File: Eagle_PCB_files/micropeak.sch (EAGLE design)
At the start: 2 parts, among them U1 ATTINY85-20MUR

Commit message: added schematic sheet template
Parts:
- added BT1: BHX1-1025-SM, BHX1-1025-SM:BHX1-1025-SM
- added LED1: (no value), led:LEDCHIPLED_0603
- added U2: MS5611-01BA03, MS5611-01BA03:MS5611-01BA03
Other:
- moved on the sheet: U$1, U1
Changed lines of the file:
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@@
 <part name="U1" library="ATTINY85-20MUR" deviceset="ATTINY85-20MUR" device=""/>
 <part name="U$1" library="CUS-12TB" deviceset="CUS-12TB" device=""/>
+<part name="U2" library="MS5611-01BA03" deviceset="MS5611-01BA03" device=""/>
+<part name="LED1" library="led" library_urn="urn:adsk.eagle:library:259" deviceset="LED" device="CHIPLED_0603" package3d_urn="urn:adsk.eagle:package:15822/2"/>
+<part name="BT1" library="BHX1-1025-SM" deviceset="BHX1-1025-SM" device=""/>
+<part name="FRAME1" library="frames" library_urn="urn:adsk.eagle:library:229" deviceset="A4L-LOC" device=""/>
 </parts>
 <sheets>
@@
 </plain>
 <instances>
-<instance part="U1" gate="G$1" x="64.77" y="38.1" smashed="yes">
-<attribute name="NAME" x="13.97" y="52.07" size="1.778" layer="95"/>
-<attribute name="VALUE" x="13.97" y="24.13" size="1.778" layer="96" rot="MR180"/>
+<instance part="U1" gate="G$1" x="140.97" y="110.49" smashed="yes">
+<attribute name="NAME" x="90.17" y="124.46" size="1.778" layer="95"/>
+<attribute name="VALUE" x="90.17" y="96.52" size="1.778" layer="96" rot="MR180"/>
 </instance>
-<instance part="U$1" gate="SW" x="167.64" y="15.24" smashed="yes">
-<attribute name="NAME" x="165.1" y="25.4" size="1.778" layer="95"/>
-<attribute name="VALUE" x="165.1" y="2.54" size="1.778" layer="96"/>
+<instance part="U$1" gate="SW" x="119.38" y="76.2" smashed="yes">
+<attribute name="NAME" x="116.84" y="86.36" size="1.778" layer="95"/>
+<attribute name="VALUE" x="116.84" y="63.5" size="1.778" layer="96"/>
+</instance>
+<instance part="U2" gate="G$1" x="45.72" y="134.62" smashed="yes">
+<attribute name="NAME" x="33.02" y="147.32" size="1.778" layer="95"/>
+<attribute name="VALUE" x="33.02" y="119.38" size="1.778" layer="96"/>
+</instance>
+<instance part="LED1" gate="G$1" x="189.23" y="77.47" smashed="yes">
+<attribute name="NAME" x="192.786" y="72.898" size="1.778" layer="95" rot="R90"/>
+<attribute name="VALUE" x="194.945" y="72.898" size="1.778" layer="96" rot="R90"/>
+</instance>
+<instance part="BT1" gate="G$1" x="57.15" y="71.12" smashed="yes">
+<attribute name="NAME" x="53.34" y="74.93" size="1.778" layer="95"/>
+<attribute name="VALUE" x="53.34" y="66.04" size="1.778" layer="96"/>
+</instance>
+<instance part="FRAME1" gate="G$1" x="0" y="0" smashed="yes">
+<attribute name="DRAWING_NAME" x="217.17" y="15.24" size="2.54" layer="94"/>
+<attribute name="LAST_DATE_TIME" x="217.17" y="10.16" size="2.286" layer="94"/>
+<attribute name="SHEET" x="230.505" y="5.08" size="2.54" layer="94"/>
 </instance>
 </instances>
@@
 </schematic>
 </drawing>
+<compatibility>
+<note version="8.2" severity="warning">
+Since Version 8.2, EAGLE supports online libraries. The ids
+of those online libraries will not be understood (or retained)
+with this version.
+</note>
+<note version="8.3" severity="warning">
+Since Version 8.3, EAGLE supports URNs for individual library
+assets (packages, symbols, and devices). The URNs of those assets
+will not be understood (or retained) with this version.
+</note>
+<note version="8.3" severity="warning">
+Since Version 8.3, EAGLE supports the association of 3D packages
+with devices in libraries, schematics, and board files. Those 3D
+packages will not be understood (or retained) with this version.
+</note>
+</compatibility>
 </eagle>

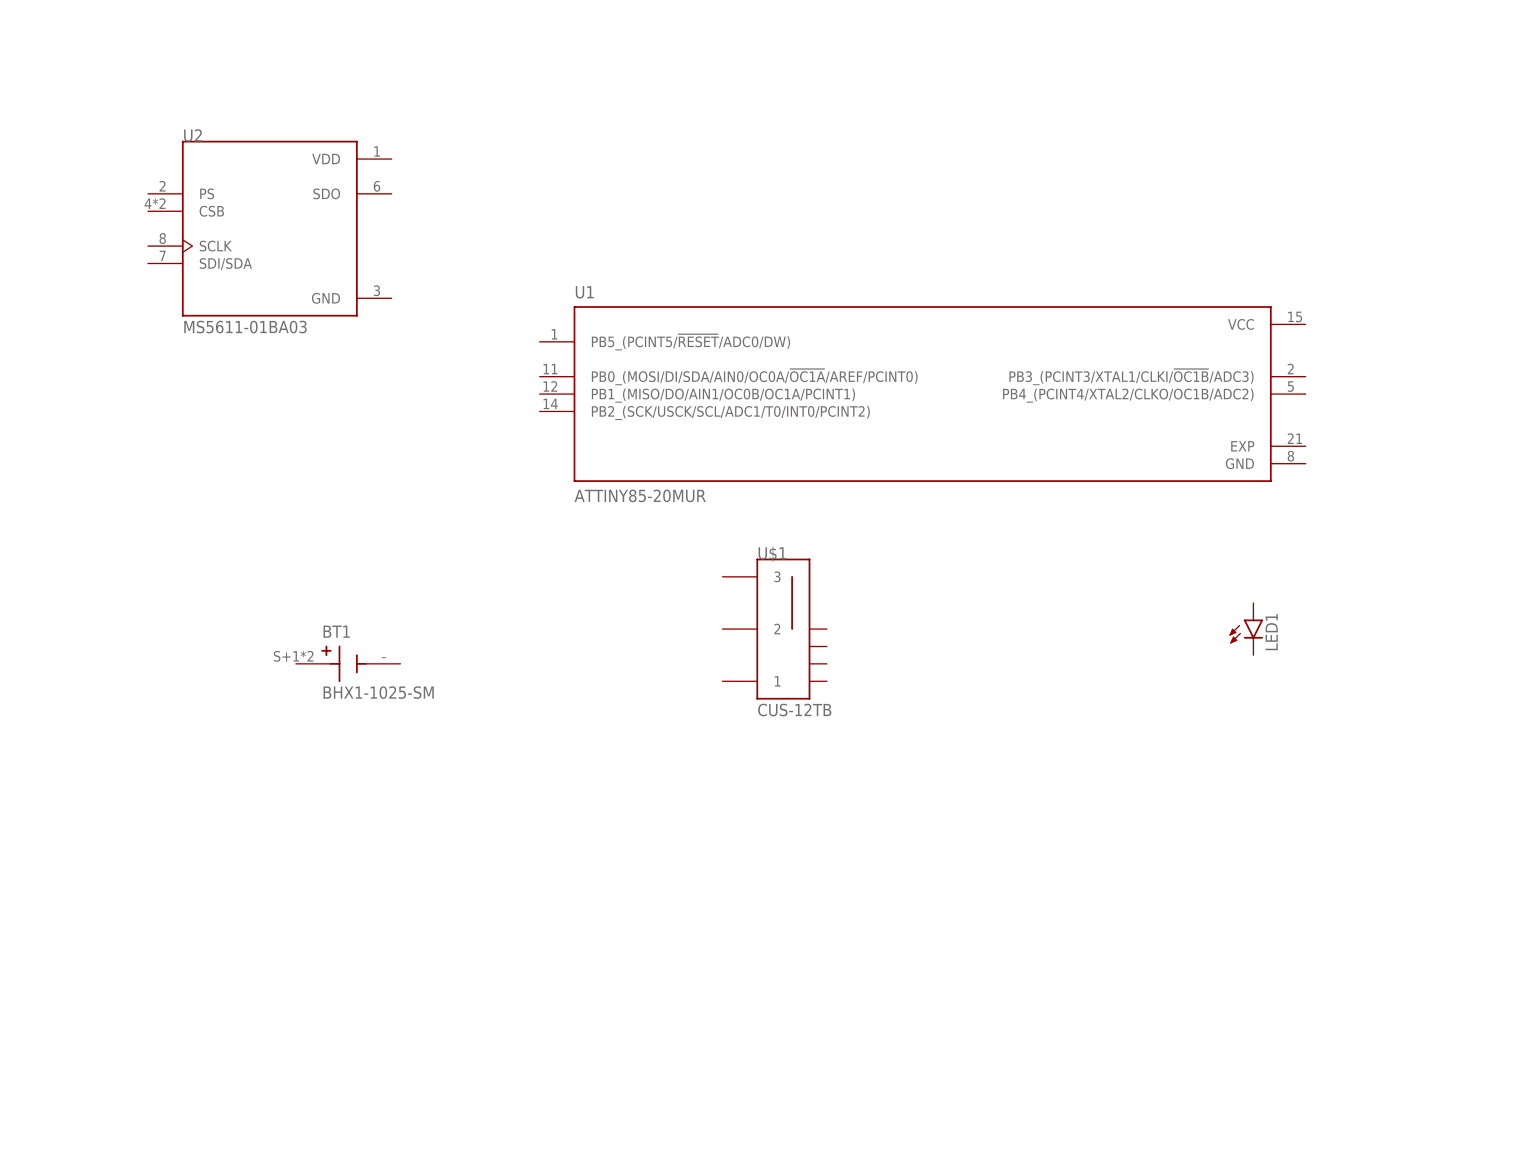
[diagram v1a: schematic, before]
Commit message: added prog header sym
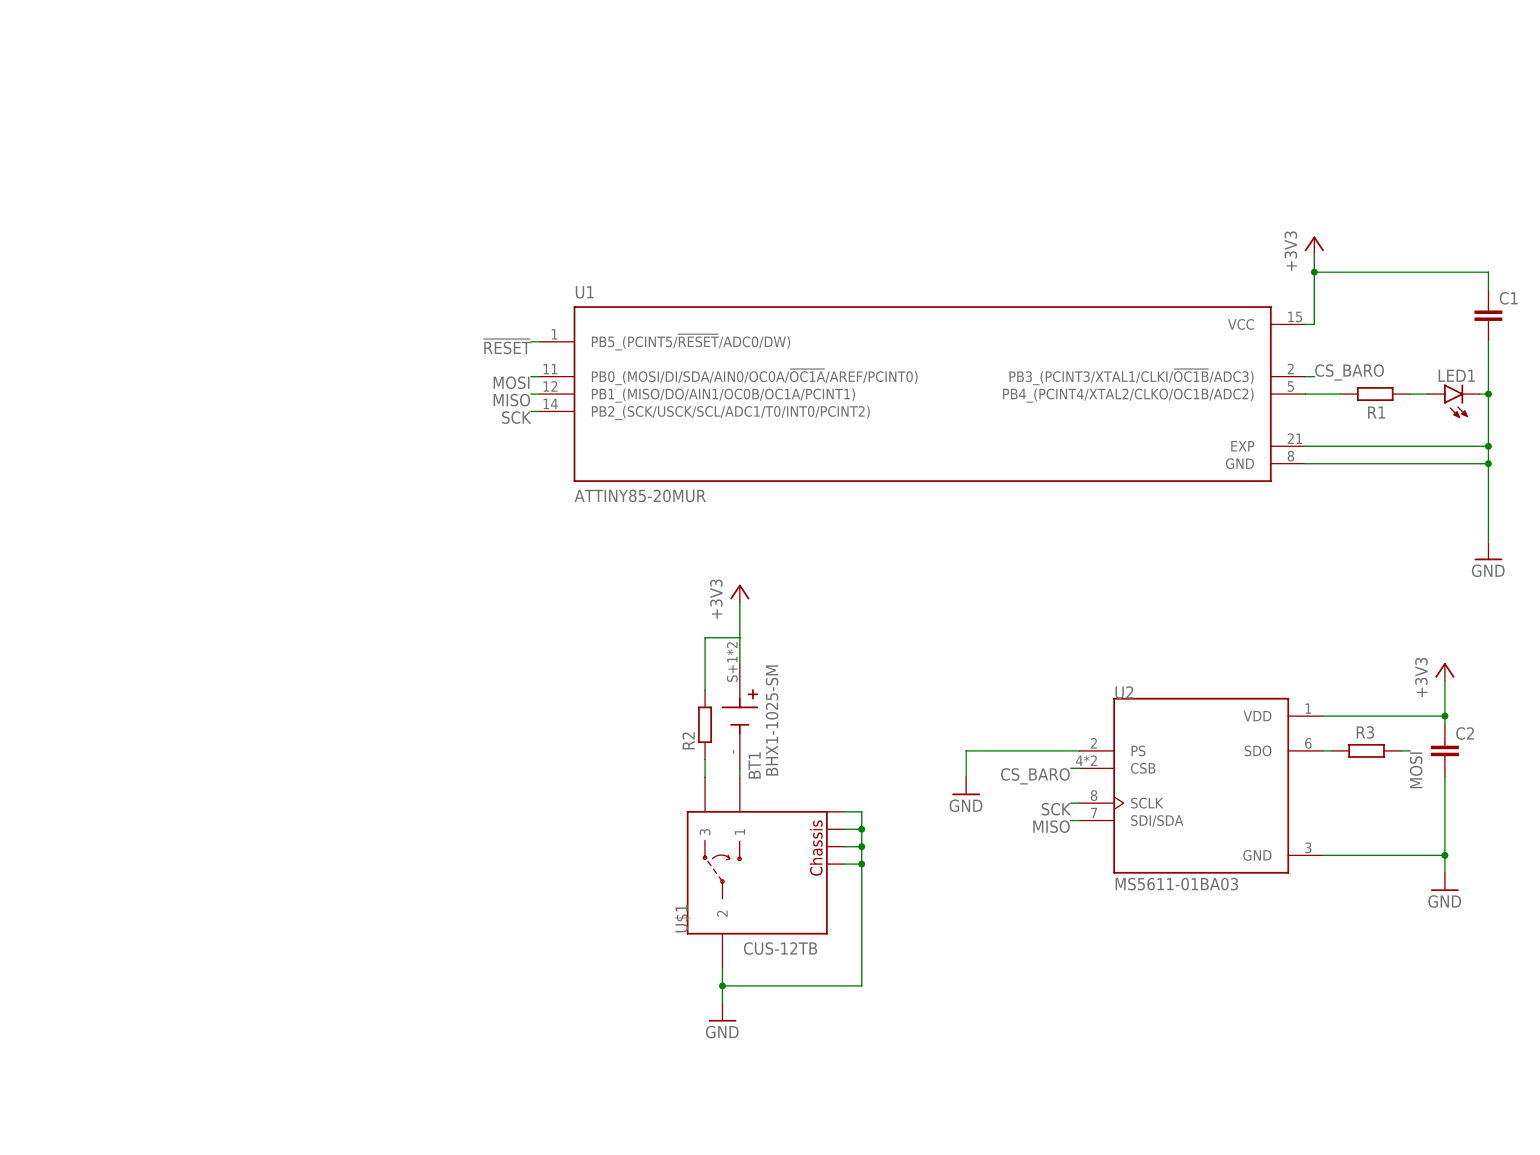
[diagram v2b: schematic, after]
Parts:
- added C1, C2: (no value), rcl:C-EUC0603
- added R1, R2, R3: (no value), rcl:R-EU_R0603
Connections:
- new net !RESET!: U1.PB5_(PCINT5/!RESET!/ADC0/DW)
- new net +3V3: BT1.+, C1.1, C2.1, R2.2, U1.VCC, U2.VDD
- new net CS_BARO: U1.PB3_(PCINT3/XTAL1/CLKI/!OC1B!/ADC3), U2.CSB
- new net GND: C1.2, C2.2, LED1.C, U$1.2, U$1.GND@1, U$1.GND@2, U$1.GND@3, U$1.GND@4, U1.EXP, U1.GND, U2.GND, U2.PS
- new net MISO: U1.PB1_(MISO/DO/AIN1/OC0B/OC1A/PCINT1), U2.SDI/SDA
- new net MOSI: R3.1, U1.PB0_(MOSI/DI/SDA/AIN0/OC0A/!OC1A!/AREF/PCINT0)
- new net N$1: BT1.-, U$1.1
- new net N$2: R2.1, U$1.3
- new net N$3: R1.1, U1.PB4_(PCINT4/XTAL2/CLKO/OC1B/ADC2)
- new net N$4: LED1.A, R1.2
- new net N$5: R3.2, U2.SDO
- new net SCK: U1.PB2_(SCK/USCK/SCL/ADC1/T0/INT0/PCINT2), U2.SCLK
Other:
- moved on the sheet: BT1, LED1, U2

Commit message: schematic done
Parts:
- added U$2: 1X6_PROG_HEADER, 1x6_prog_header:1X6_PROG_HEADER
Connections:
- net !RESET!: now also U$2.P$5
- net +3V3: now also U$2.P$2
- net GND: now also U$2.P$6
- net MISO: now also U$2.P$1
- net MOSI: now also U$2.P$4
- net SCK: now also U$2.P$3
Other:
- note added: "ATTINY85 MCU"
- note added: "Barometer"
- note added: "ON/OFF Switch"
- note added: "Programming Header"
- moved on the sheet: BT1, C1, C2, LED1, R1, R2, R3, U$1, U1, U2

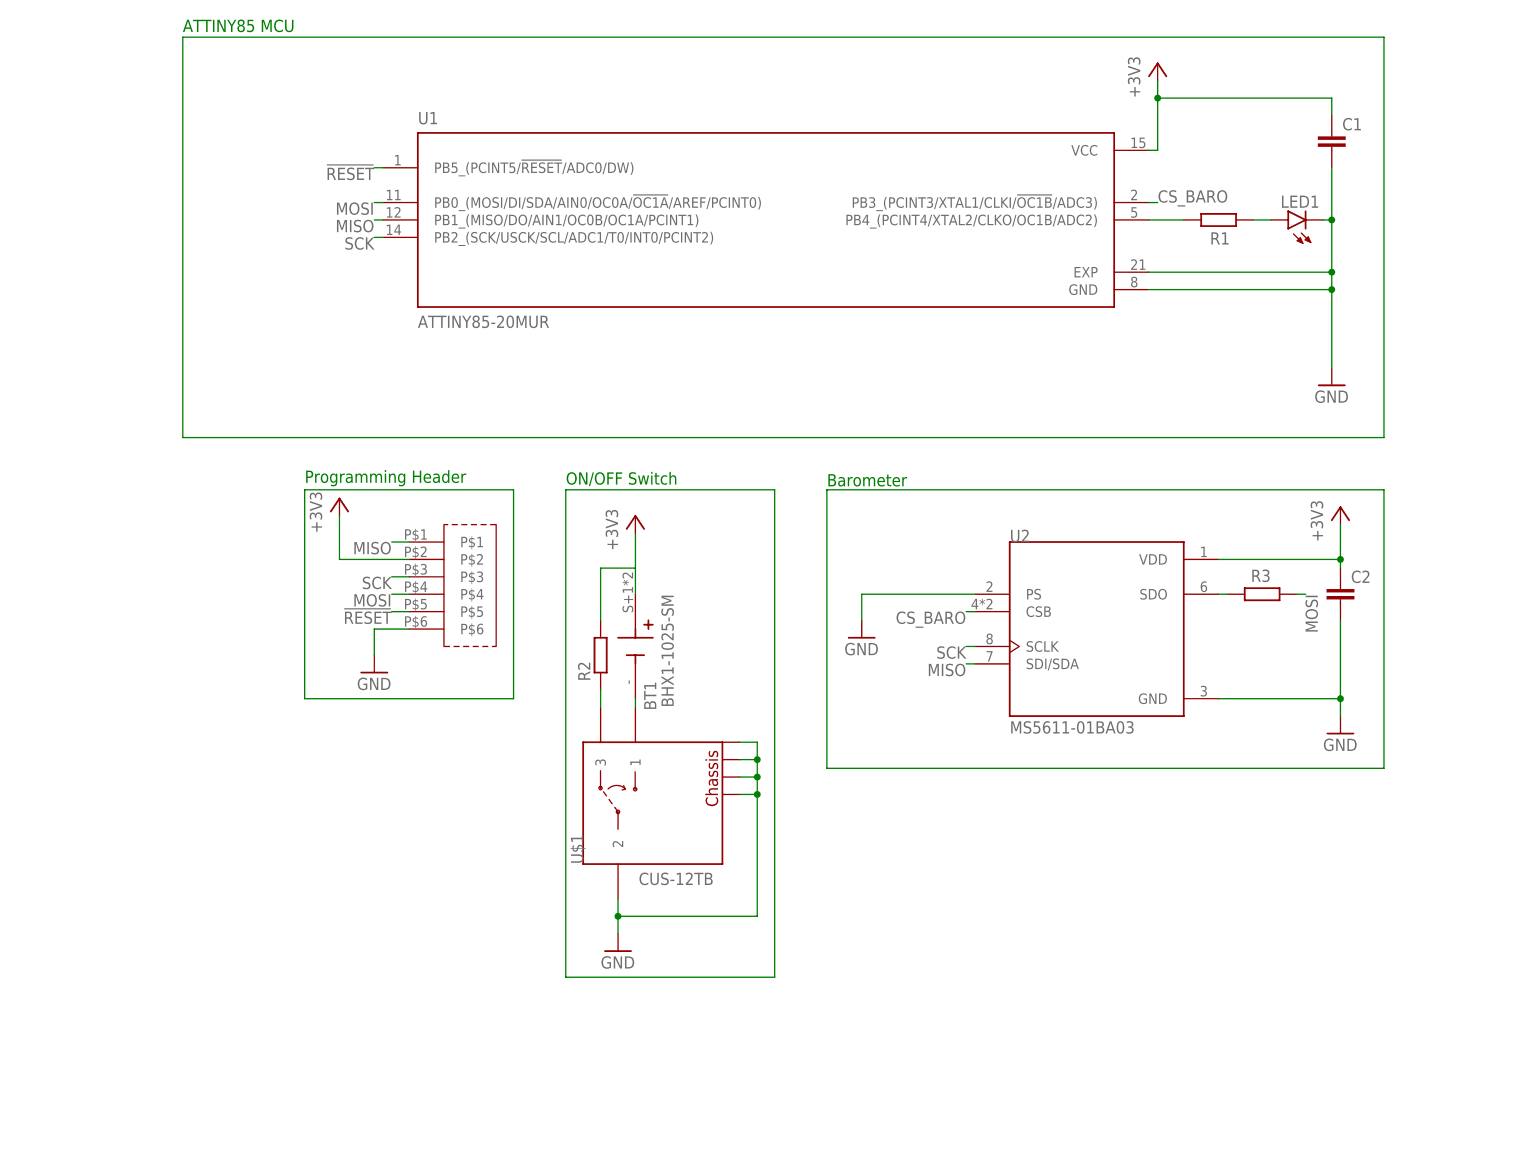
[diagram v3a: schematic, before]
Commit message: scaled board image incorrecly, smd pads actually 0.5x0.9mm
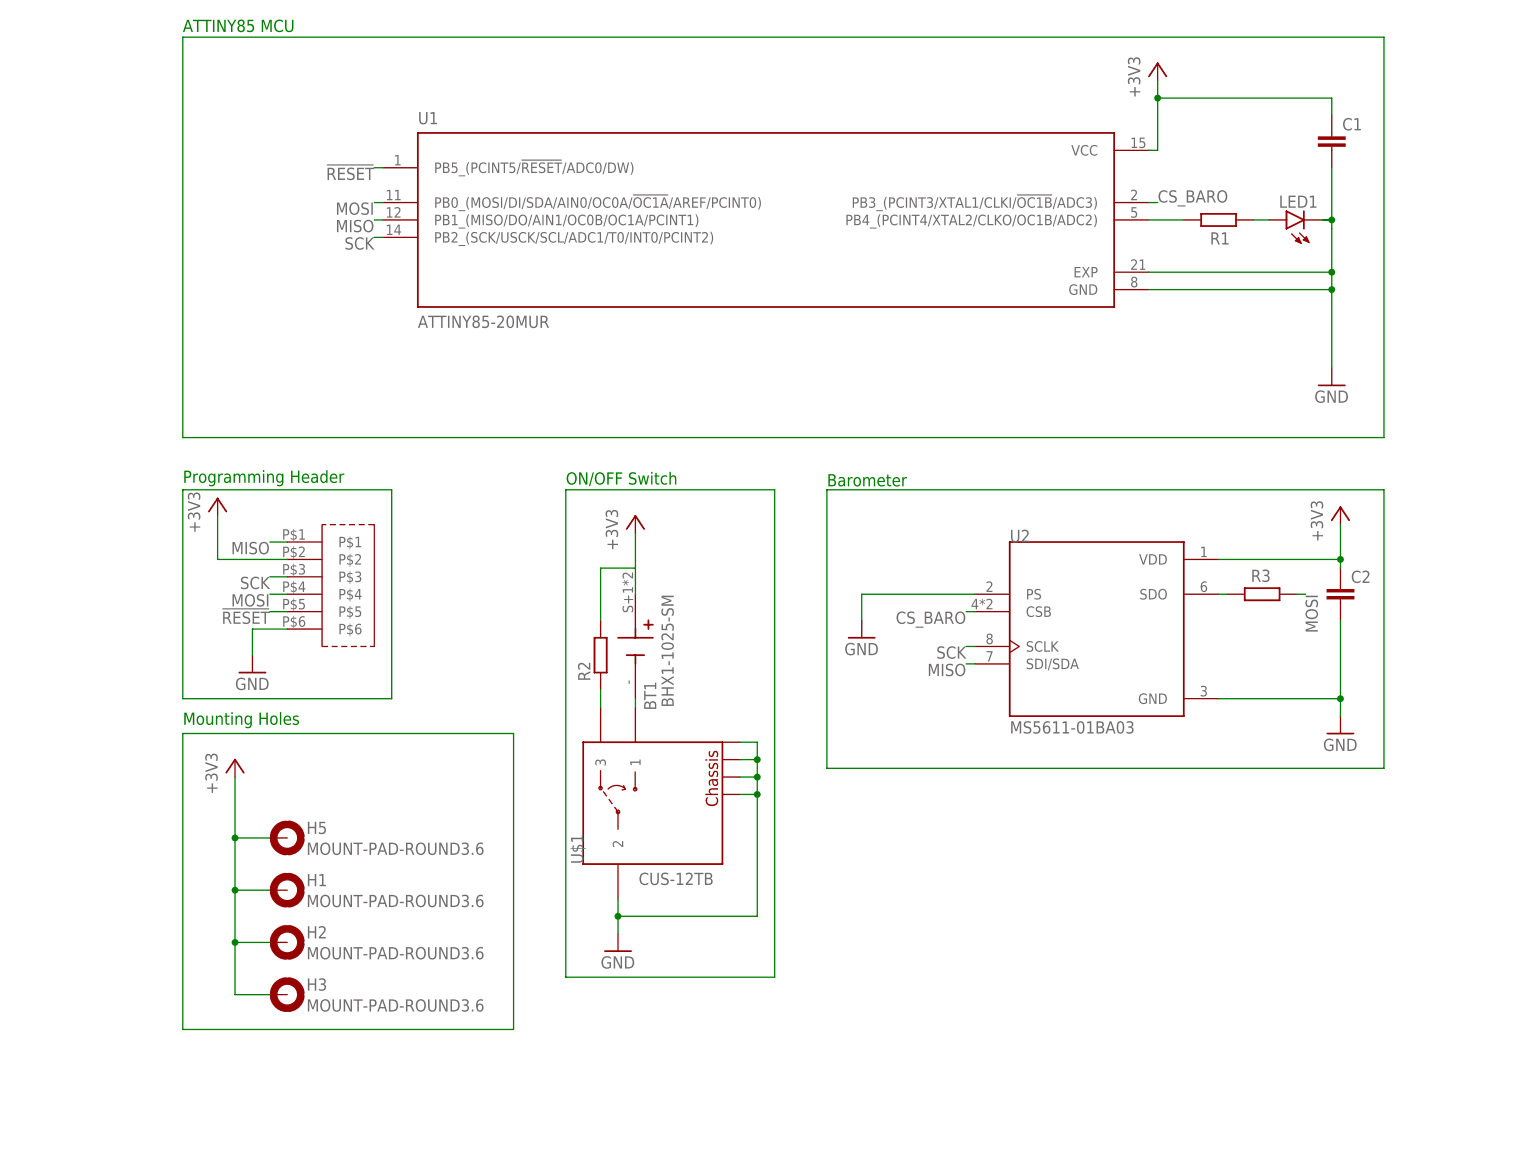
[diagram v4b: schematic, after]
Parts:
- added H1, H2, H3, H5: MOUNT-PAD-ROUND3.6, holes:MOUNT-PAD-ROUND3.6
- LED1: device led:LEDCHIPLED_0603 -> led:LEDP-LCC-2
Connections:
- net +3V3: now also H1.MOUNT, H2.MOUNT, H3.MOUNT, H5.MOUNT
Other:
- note added: "Mounting Holes"
